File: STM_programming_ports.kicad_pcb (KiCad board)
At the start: 2 copper layers, 68.6 x 38.1 mm, 6 parts, among them J1 Conn_ARM_JTAG_SWD_10, J2 Conn_ARM_JTAG_SWD_20, J3 Conn_01x02_Male, J4 Conn_01x04_Female, U1 st-linkv2-clone-port, U2 st-linkv2-clone-port

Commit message: Version02
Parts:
- removed U1, U2: st-linkv2-clone-port, Connector_IDC:IDC-Header_2x05_P2.54mm_Vertical
- added D1: Red, LED_SMD:LED_1206_3216Metric_Pad1.42x1.75mm_HandSolder, F.Cu at (144.0, 63.0)
- added J5: 6PinDebugPort, Connector_IDC:IDC-Header_2x03_P2.54mm_Vertical, F.Cu at (120.0, 64.5)
- added J6: FOUR_WIRE_CONN, Connector_PinHeader_2.54mm:PinHeader_1x04_P2.54mm_Vertical, F.Cu at (104.0, 66.5)
- added J7: st-linkv2-clone-port, Connector_IDC:IDC-Header_2x05_P2.54mm_Vertical, F.Cu at (148.0, 45.5)
- added J8: SW_WITH_RST, Connector_PinHeader_2.54mm:PinHeader_1x05_P2.54mm_Vertical, F.Cu at (88.0, 66.5)
- added R1: 3K9, Resistor_SMD:R_1206_3216Metric_Pad1.30x1.75mm_HandSolder, F.Cu at (144.0, 66.0)
- added SW1: SW_Push, custom_buttons_switches:TSB008, F.Cu at (154.5, 67.5)
- J2: value Conn_ARM_JTAG_SWD_20 -> st-linkv2-clone-port; footprint Connector_IDC:IDC-Header_2x10_P2.54mm_Vertical -> Connector_IDC:IDC-Header_2x05_P2.54mm_Horizontal
- J3: value Conn_01x02_Male -> Conn_ARM_JTAG_SWD_20; footprint Connector_PinHeader_2.54mm:PinHeader_1x02_P2.54mm_Vertical -> Connector_IDC:IDC-Header_2x10_P2.54mm_Vertical
- J4: value Conn_01x04_Female -> Conn_01x02_Male; footprint Connector_PinHeader_2.54mm:PinHeader_1x04_P2.54mm_Vertical -> Connector_PinHeader_2.54mm:PinHeader_1x02_P2.54mm_Vertical
- moved J2 68.6 mm to (157.5, 47.5)
- moved J3 41.5 mm to (103.0, 48.3), turned to 90 degrees
- moved J4 27.4 mm to (137.0, 63.0), turned to 0 degrees
- moved J1 24.5 mm to (80.9, 48.5), turned to 90 degrees
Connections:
- J1 pad 7: Net-(J1-Pad7) -> (no net)
- J1 pad 8: Net-(J1-Pad8) -> (no net)
- J2 pad 1: +3V3 -> /RST
- J2 pad 10: GND -> (no net)
- J2 pad 2: +3V3 -> /SWDIO
- J2 pad 3: Net-(J2-Pad3) -> GND
- J2 pad 5: Net-(J2-Pad5) -> /SWIM
- J2 pad 6: GND -> /SWCLK
- J2 pad 7: /SWDIO -> Net-(J2-Pad7)
- J2 pad 8: GND -> Net-(J2-Pad7)
- J2 pad 9: /SWCLK -> (no net)
- J3 pad 1: Net-(J3-Pad1) -> +3V3
- J4 pad 1: +3V3 -> Net-(J2-Pad7)
- J4 pad 2: /SWDIO -> +3V3
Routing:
- net /RST: track 63.7 -> 120.1 mm, vias 1 -> 3
- net /SWDIO: track 87.7 -> 134.9 mm, vias 0 -> 4
- net /SWCLK: track 83.6 -> 129.6 mm, vias 0 -> 4
- net /SWIM: track 57.3 -> 103.1 mm, vias 0 -> 4
- net +3V3: track 84.0 -> 124.6 mm, vias 0 -> 2
- net Net-(J2-Pad7): track 0.00 -> 26.3 mm
- net Net-(J3-Pad1): track 21.2 -> 0.00 mm
- net Net-(D1-Pad2): track 0.00 -> 3.03 mm
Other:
- board size 68.6 x 38.1 mm -> 87.5 x 30 mm
- board text added: "10 Pin JTAG Port"
- board text added: "20 pin JTAG Port"
- board text added: "4 WIre SW"
- board text added: "6 Pin DBG Port"
- board text added: "Gnd"
- board text added: "JLCJLCJLCJLC"
- board text added: "PWR JUMPER"
- board text added: "PWR LED"
- board text added: "RST"
- board text added: "RST BTN"
- board text added: "ST-Link Clone"
- board text added: "STM32 Programming Ports V02 By MKrysz"
- board text added: "SW with RST"
- board text removed: "10-pin JTAG"
- board text removed: "20-pin JTAG"
- board text removed: "GND"
- board text removed: "Input"
- board text removed: "Power"
- board text removed: "ST-Link clone"
- board text removed: "STM32_programming_ports by MKrysz"
- board text removed: "V01"

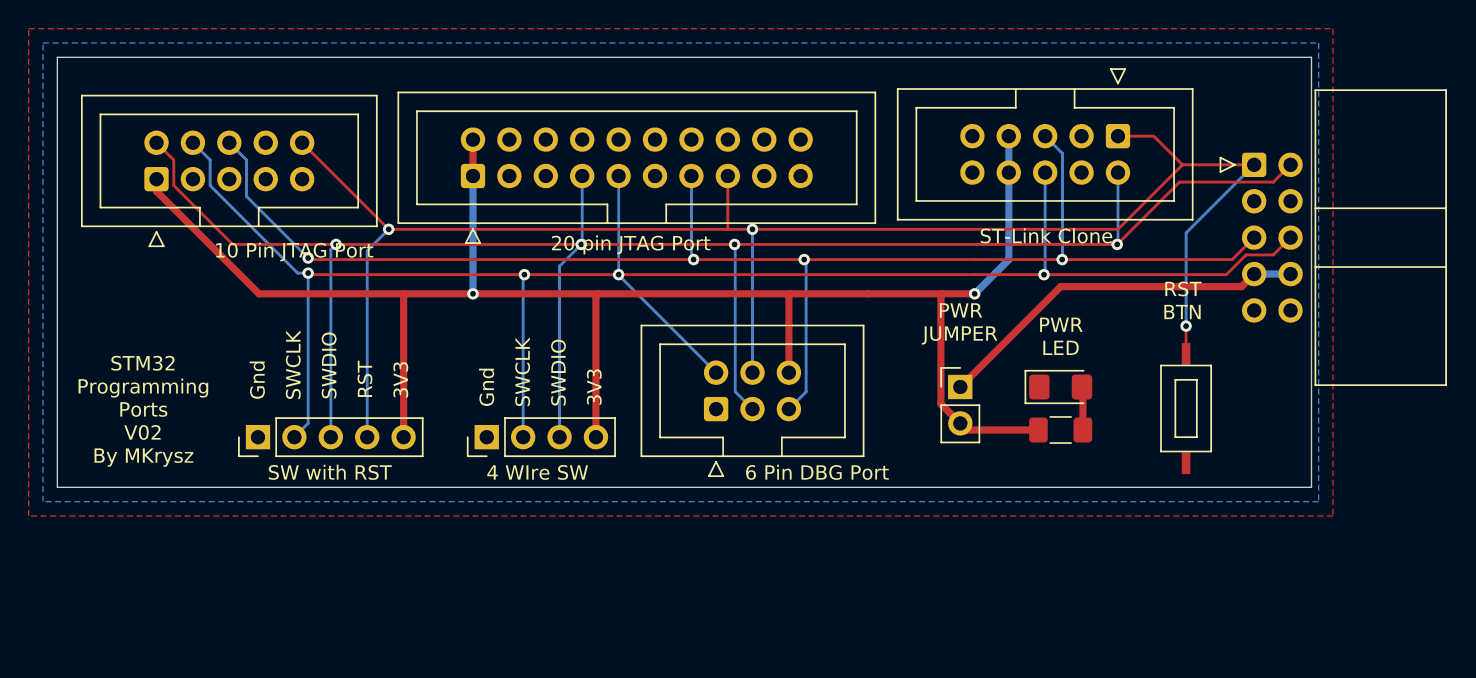
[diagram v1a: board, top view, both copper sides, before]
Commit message: Minor position changes
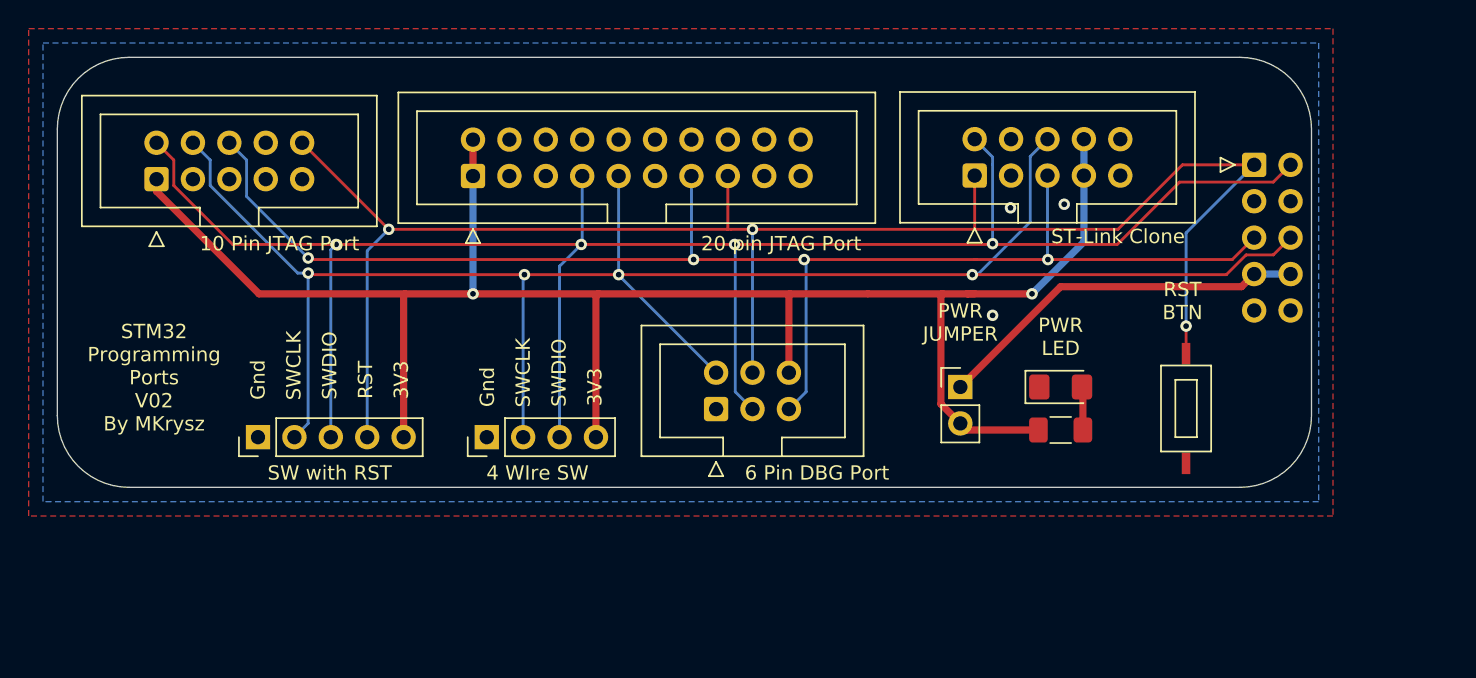
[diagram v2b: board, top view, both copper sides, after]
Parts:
- moved J7 10.4 mm to (138.0, 48.2), turned to 90 degrees
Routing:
- net +3V3: track 124.6 -> 130.0 mm
- net /SWCLK: track 129.6 -> 134.3 mm
- net /SWIM: track 103.1 -> 99.9 mm
- net /SWDIO: track 134.9 -> 137.8 mm
- net /RST: track 120.1 -> 118.5 mm
- net GND: vias 0 -> 3
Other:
- outline, holes or cut-outs redrawn
